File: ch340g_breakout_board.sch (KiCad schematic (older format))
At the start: 6 parts, among them J1 Conn_01x08_Male, J2 Conn_01x08_Male, U1 CH340G, Y1 12Mhz

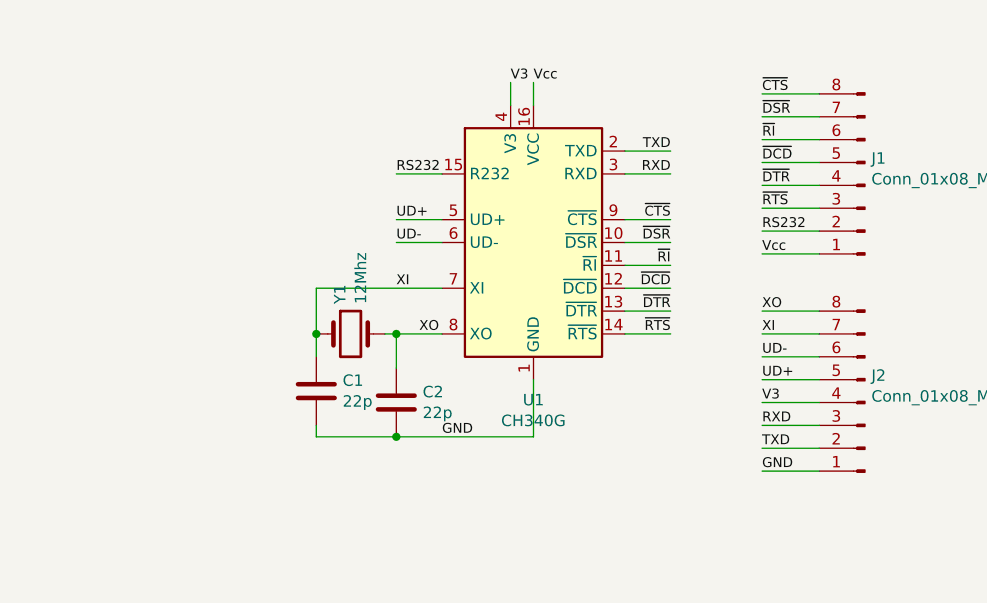
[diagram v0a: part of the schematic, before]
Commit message: Updated to REV2: Includes USB-Mini B connector
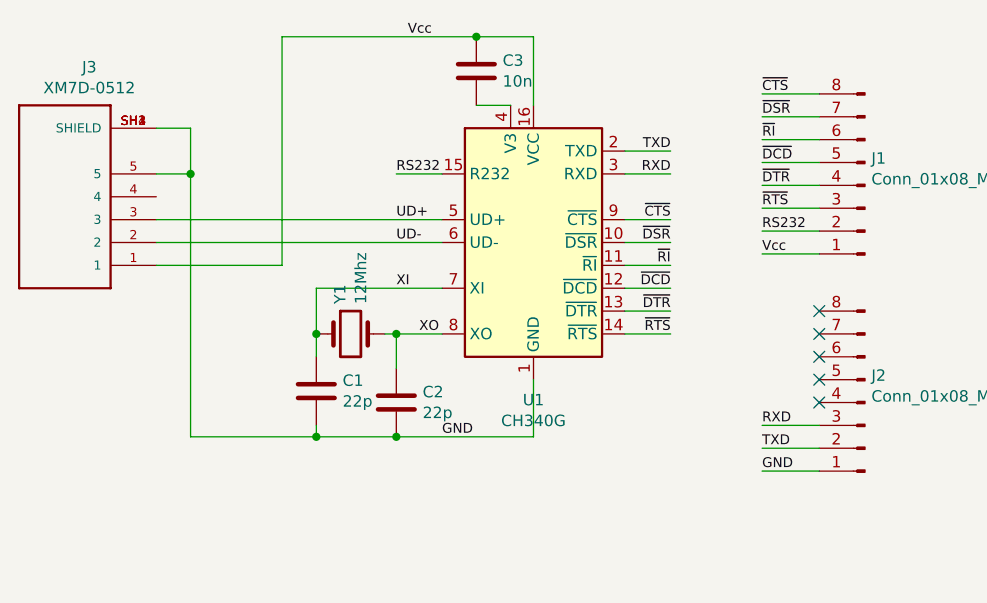
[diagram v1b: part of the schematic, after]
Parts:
- added C3: 10n, Capacitor_THT:C_Disc_D3.0mm_W1.6mm_P2.50mm, symbol Device:C
- added J3: XM7D-0512, OMRON_XM7D-0512, symbol XM7D-0512:XM7D-0512
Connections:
- net GND: now also J3.5, J3.SH1 (SHIELD), J3.SH2 (SHIELD), J3.SH3 (SHIELD), J3.SH4 (SHIELD)
- net UD+: now also J3.3; no longer J2.5 (Pin_5)
- net UD-: now also J3.2; no longer J2.6 (Pin_6)
- net Vcc: now also C3.1, J3.1
- net XI: no longer J2.7 (Pin_7)
- net XO: no longer J2.8 (Pin_8)
- net V3: no longer names the net of U1.4 (V3)
- net V3: now also C3.2; no longer J2.4 (Pin_4)
- no-connect marks 0 -> 5
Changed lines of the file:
@@
 Title ""
 Date ""
-Rev ""
+Rev "2"
 Comp ""
 Comment1 ""
@@
 	1    0    0    -1
 $EndComp
-Text Label 4650 2400 0    43   ~ 0
+Text Label 4100 2200 0    43   ~ 0
 Vcc
 Text Label 5650 2450 0    43   ~ 0
@@
 Wire Wire Line
 	4250 2800 4050 2800
-Wire Wire Line
-	4650 2400 4650 2500
 Text Label 5650 4100 0    43   ~ 0
 GND
@@
 Text Label 5650 3900 0    43   ~ 0
 RXD
-Text Label 5650 3800 0    43   ~ 0
-V3
-Text Label 5650 3700 0    43   ~ 0
-UD+
-Text Label 5650 3600 0    43   ~ 0
-UD-
-Text Label 5650 3500 0    43   ~ 0
-XI
-Text Label 5650 3400 0    43   ~ 0
-XO
-Wire Wire Line
-	5650 3400 5900 3400
-Wire Wire Line
-	5900 3500 5650 3500
-Wire Wire Line
-	5650 3600 5900 3600
-Wire Wire Line
-	5900 3700 5650 3700
-Wire Wire Line
-	5650 3800 5900 3800
 Wire Wire Line
 	5900 3900 5650 3900
@@
 Text Label 5250 2800 2    43   ~ 0
 RXD
-Text Label 4550 2400 0    43   ~ 0
-V3
 Text Label 4050 3000 0    43   ~ 0
 UD+
@@
 Wire Wire Line
 	5250 2800 5050 2800
-Wire Wire Line
-	4550 2400 4550 2500
-Wire Wire Line
-	4050 3000 4250 3000
-Wire Wire Line
-	4050 3100 4250 3100
+Connection ~ 3700 3950
+Wire Wire Line
+	4650 2200 4650 2500
+$Comp
+L XM7D-0512:XM7D-0512 J3
+U 1 1 5EB6D036
+P 2600 2900
+F 0 "J3" H 2493 2333 50  0000 C CNN
+F 1 "XM7D-0512" H 2493 2424 50  0000 C CNN
+F 2 "OMRON_XM7D-0512" H 2600 2900 50  0001 L BNN
+F 3 "Manufacturer recommendations" H 2600 2900 50  0001 L BNN
+F 4 "OMRON" H 2600 2900 50  0001 L BNN "Field4"
+F 5 "" H 2600 2900 50  0001 L BNN "Field5"
+	1    2600 2900
+	-1   0    0    1
+$EndComp
+Wire Wire Line
+	4250 3000 3000 3000
+Wire Wire Line
+	4250 3100 3000 3100
+Wire Wire Line
+	3000 3200 3550 3200
+Wire Wire Line
+	3550 2200 3550 3200
+Wire Wire Line
+	3000 2600 3150 2600
+Wire Wire Line
+	3150 2600 3150 2800
+Wire Wire Line
+	3150 2800 3000 2800
+Wire Wire Line
+	3150 2800 3150 3950
+Connection ~ 3150 2800
+Wire Wire Line
+	3150 3950 3700 3950
+NoConn ~ 5900 3400
+NoConn ~ 5900 3500
+NoConn ~ 5900 3600
+NoConn ~ 5900 3700
+$Comp
+L Device:C C3
+U 1 1 5EB8F05F
+P 4400 2350
+F 0 "C3" H 4515 2396 50  0000 L CNN
+F 1 "10n" H 4515 2305 50  0000 L CNN
+F 2 "Capacitor_THT:C_Disc_D3.0mm_W1.6mm_P2.50mm" H 4438 2200 50  0001 C CNN
+F 3 "~" H 4400 2350 50  0001 C CNN
+	1    4400 2350
+	1    0    0    -1
+$EndComp
+Connection ~ 4400 2200
+Wire Wire Line
+	4400 2200 4650 2200
+Wire Wire Line
+	4400 2500 4550 2500
+Wire Wire Line
+	3550 2200 4400 2200
+NoConn ~ 5900 3800
 $EndSCHEMATC
